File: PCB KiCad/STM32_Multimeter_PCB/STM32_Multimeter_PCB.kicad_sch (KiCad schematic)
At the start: 57 parts, among them J1 Conn_01x02_Pin, J2 USB_B_Micro, J3 Conn_01x04_Pin, J4 Conn_Coaxial, J5 Conn_01x03_Pin, SW1 SW_Push, SW3 SW_Push, SW4 SW_DPDT_x2, U1 STM32WB55CGUx, U10 AMS1117-3.3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

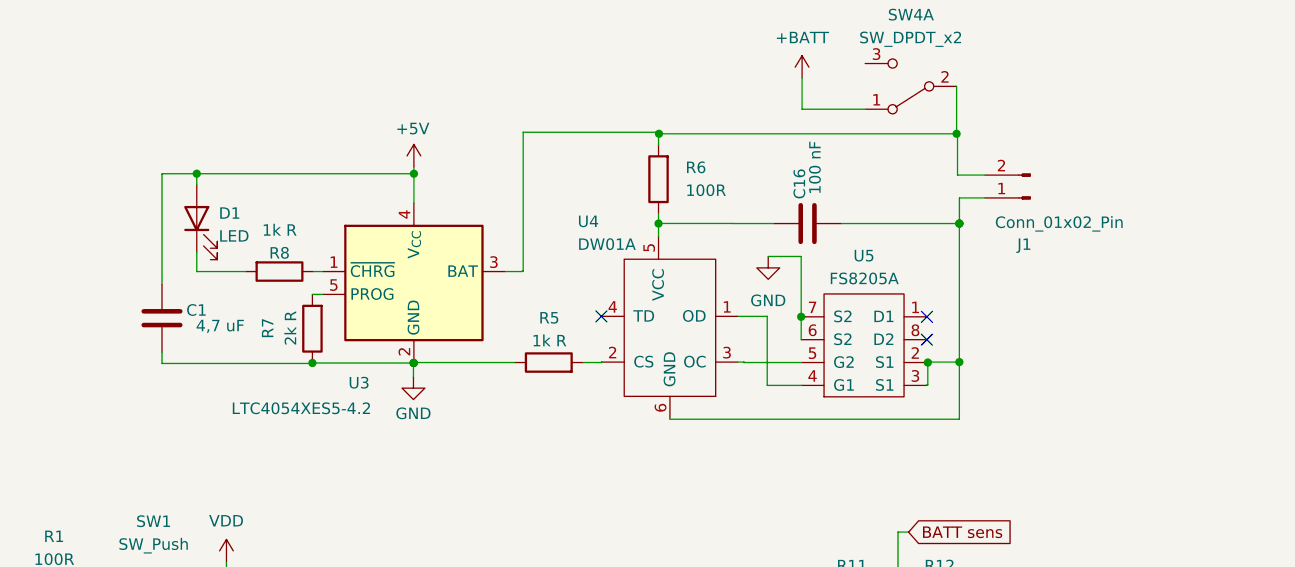
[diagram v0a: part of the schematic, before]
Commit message: Routed Analog and Microcontroler section
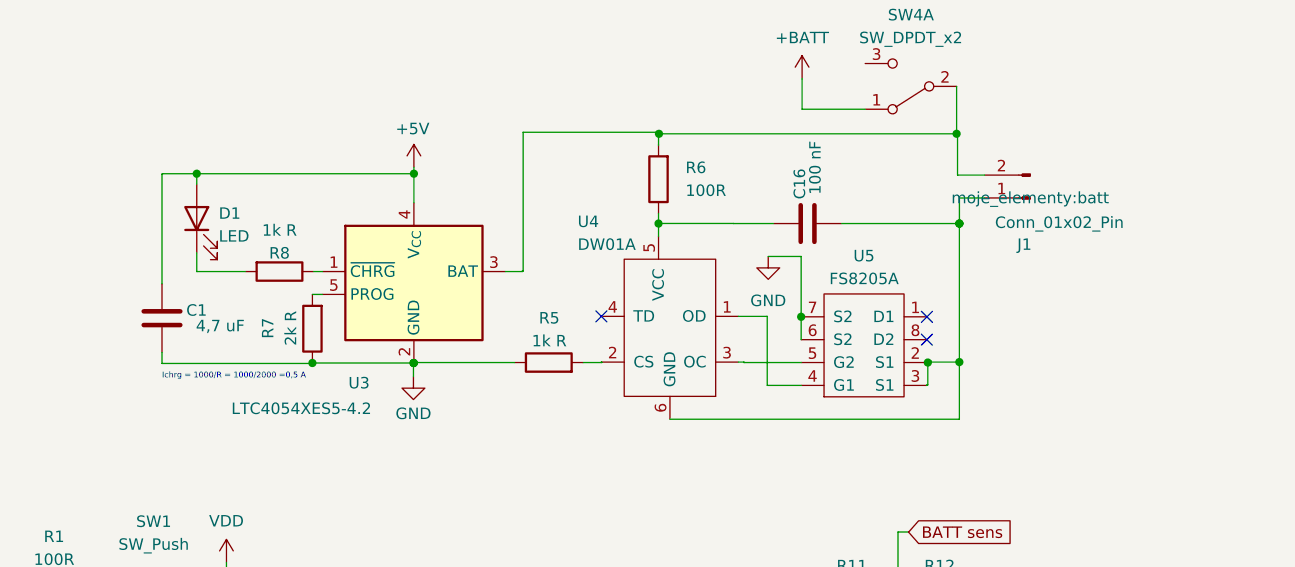
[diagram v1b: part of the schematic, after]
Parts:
- J1: footprint Connector_PinHeader_2.54mm:PinHeader_1x02_P2.54mm_Vertical -> moje_elementy:batt
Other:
- note added: "Ichrg = 1000/R = 1000/2000 =0,5 A"
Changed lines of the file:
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@@
     (stroke (width 0) (type default))
+  )
+  (text "Ichrg = 1000/R = 1000/2000 =0,5 A" (at 173.7868 54.2544 0)
+    (effects (font (size 0.64 0.64)) (justify left bottom))
   )
   (text "Lowpass filter \nfc=1/(2pi(LC)^1/2)=\n1/(2pi(10*10^-6*4,7*10^-6)^1/2)=\n23,22 kHz"
@@
       (effects (font (size 1.27 1.27)))
     )
-    (property "Footprint" "Connector_PinHeader_2.54mm:PinHeader_1x02_P2.54mm_Vertical" (at 270.256 33.9852 0)
-      (effects (font (size 1.27 1.27)) hide)
+    (property "Footprint" "moje_elementy:batt" (at 270.256 33.9852 0)
+      (effects (font (size 1.27 1.27)))
     )
     (property "Datasheet" "~" (at 270.256 33.9852 0)

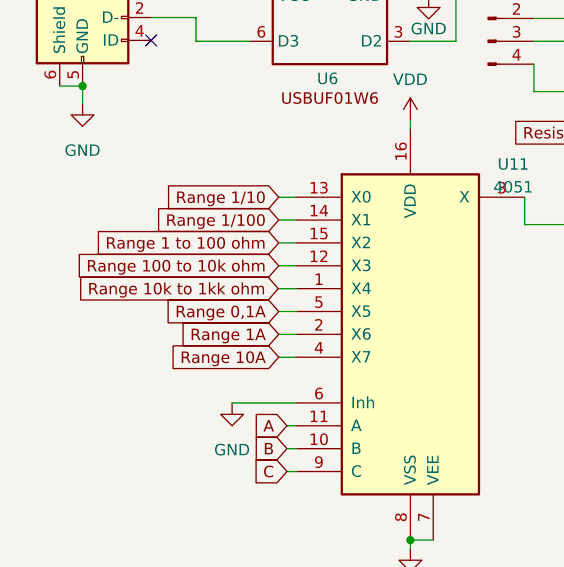
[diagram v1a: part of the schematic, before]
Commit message: routed out signals and power planes
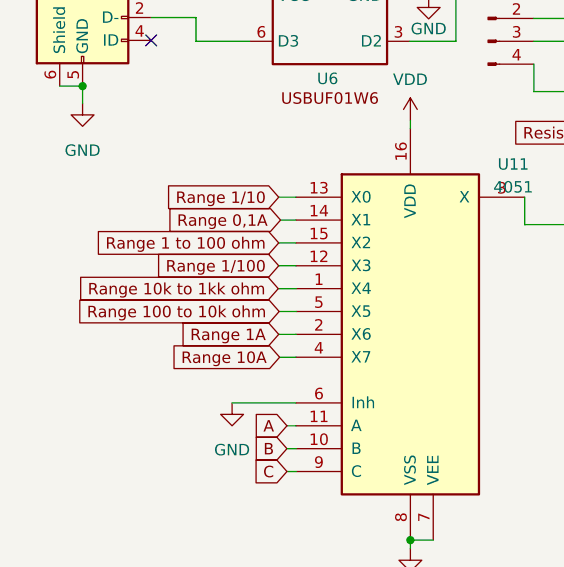
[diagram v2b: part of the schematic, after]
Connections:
- net Range 0,1A: now also U11.14 (X1); no longer U11.5 (X5)
- net Range 100 to 10k ohm: now also U11.5 (X5); no longer U11.12 (X3)
- net Range 1/100: now also U11.12 (X3); no longer U11.14 (X1)
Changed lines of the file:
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@@
-    (stroke (width 0) (type default))
-  )
-  (wire (pts (xy 44.2468 151.5364) (xy 42.3164 151.5364))
     (stroke (width 0) (type default))
   )
@@
     (stroke (width 0) (type default))
   )
-  (wire (pts (xy 44.2468 159.1564) (xy 42.3164 159.1564))
+  (wire (pts (xy 42.3672 164.2364) (xy 44.2468 164.2364))
     (stroke (width 0) (type default))
   )
@@
     (stroke (width 0) (type default))
   )
+  (wire (pts (xy 42.418 169.3164) (xy 44.2468 169.3164))
+    (stroke (width 0) (type default))
+  )
   (wire (pts (xy 69.4944 32.9692) (xy 69.4944 32.3342))
     (stroke (width 0) (type default))
@@
     (stroke (width 0) (type default))
   )
+  (wire (pts (xy 42.5196 154.0764) (xy 44.2468 154.0764))
+    (stroke (width 0) (type default))
+  )
   (wire (pts (xy 47.752 114.4016) (xy 47.752 115.7732))
     (stroke (width 0) (type default))
@@
     (stroke (width 0) (type default))
   )
-  (wire (pts (xy 44.2468 154.0764) (xy 42.3164 154.0764))
-    (stroke (width 0) (type default))
-  )
   (wire (pts (xy 251.9172 24.13) (xy 244.9068 24.13))
     (stroke (width 0) (type default))
@@
     (stroke (width 0) (type default))
   )
-  (wire (pts (xy 44.2468 164.2364) (xy 42.3164 164.2364))
-    (stroke (width 0) (type default))
-  )
   (wire (pts (xy 122.5804 43.1371) (xy 122.5296 43.1371))
     (stroke (width 0) (type default))
@@
     (stroke (width 0) (type default))
   )
+  (wire (pts (xy 42.3164 159.1564) (xy 44.2468 159.1564))
+    (stroke (width 0) (type default))
+  )
   (wire (pts (xy 139.7508 121.5644) (xy 129.032 121.5644))
     (stroke (width 0) (type default))
@@
     (stroke (width 0) (type default))
   )
-  (wire (pts (xy 42.3164 169.3164) (xy 44.2468 169.3164))
-    (stroke (width 0) (type default))
-  )
   (wire (pts (xy 29.8704 123.952) (xy 29.8704 122.2248))
     (stroke (width 0) (type default))
@@
   )
   (wire (pts (xy 87.7824 73.66) (xy 98.5012 73.66))
+    (stroke (width 0) (type default))
+  )
+  (wire (pts (xy 42.3164 151.5364) (xy 44.2468 151.5364))
     (stroke (width 0) (type default))
   )
@@
     (effects (font (size 0.54 0.54)) (justify left bottom))
   )
-  (global_label "Range 100 to 10k ohm" (shape input) (at 42.3164 159.1564 180) (fields_autoplaced)
-    (effects (font (size 1.27 1.27)) (justify right))
-    (property "Intersheetrefs" "${INTERSHEET_REFS}" (at 16.7136 159.1564 0)
+  (global_label "Range 100 to 10k ohm" (shape input) (at 42.3672 164.2364 180) (fields_autoplaced)
+    (effects (font (size 1.27 1.27)) (justify right))
+    (property "Intersheetrefs" "${INTERSHEET_REFS}" (at 16.7644 164.2364 0)
       (effects (font (size 1.27 1.27)) (justify right) hide)
     )
@@
     )
   )
-  (global_label "Range 1{slash}100" (shape input) (at 42.3164 154.0764 180) (fields_autoplaced)
-    (effects (font (size 1.27 1.27)) (justify right))
-    (property "Intersheetrefs" "${INTERSHEET_REFS}" (at 26.3895 154.0764 0)
-      (effects (font (size 1.27 1.27)) (justify right) hide)
-    )
-  )
-  (global_label "Range 0,1A" (shape input) (at 42.3164 164.2364 180) (fields_autoplaced)
-    (effects (font (size 1.27 1.27)) (justify right))
-    (property "Intersheetrefs" "${INTERSHEET_REFS}" (at 28.4456 164.2364 0)
+  (global_label "Range 1{slash}100" (shape input) (at 42.3164 159.1564 180) (fields_autoplaced)
+    (effects (font (size 1.27 1.27)) (justify right))
+    (property "Intersheetrefs" "${INTERSHEET_REFS}" (at 26.3895 159.1564 0)
+      (effects (font (size 1.27 1.27)) (justify right) hide)
+    )
+  )
+  (global_label "Range 0,1A" (shape input) (at 42.5196 154.0764 180) (fields_autoplaced)
+    (effects (font (size 1.27 1.27)) (justify right))
+    (property "Intersheetrefs" "${INTERSHEET_REFS}" (at 28.6488 154.0764 0)
       (effects (font (size 1.27 1.27)) (justify right) hide)
     )
@@
     )
   )
-  (global_label "Range 10A" (shape input) (at 42.3164 169.3164 180) (fields_autoplaced)
-    (effects (font (size 1.27 1.27)) (justify right))
-    (property "Intersheetrefs" "${INTERSHEET_REFS}" (at 29.0504 169.3164 0)
-      (effects (font (size 1.27 1.27)) (justify right) hide)
-    )
+  (global_label "Range 10A" (shape input) (at 42.418 169.3164 180) (fields_autoplaced)
+    (effects (font (size 1.27 1.27)) (justify right))
+    (property "Intersheetrefs" "${INTERSHEET_REFS}" (at 29.152 169.3164 0)
+      (effects (font (size 1.27 1.27)) (justify right) hide)
+    )

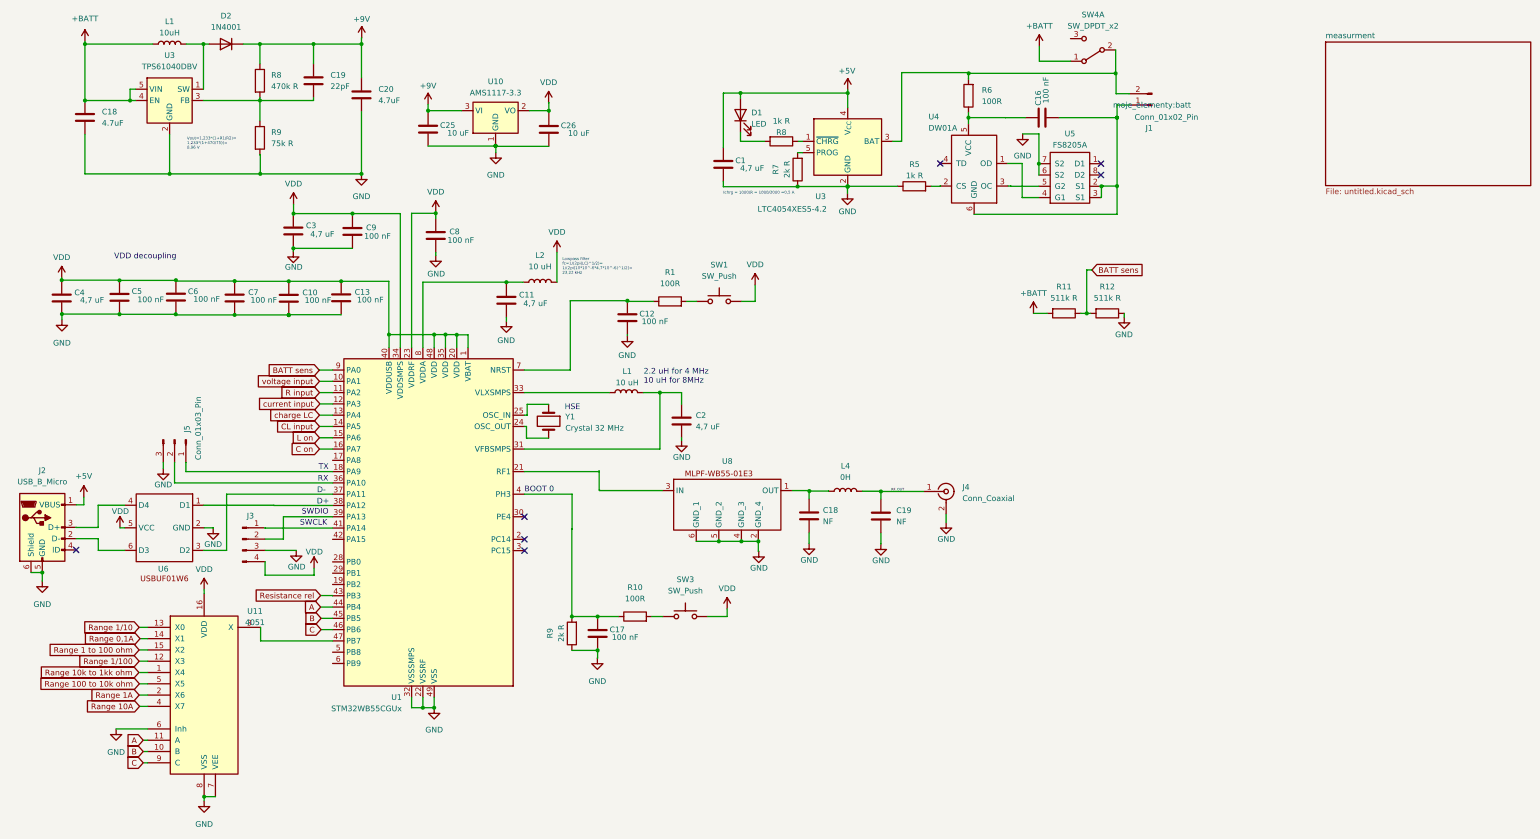
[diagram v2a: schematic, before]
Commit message: added i2c for oled and 2 buttons to pcb
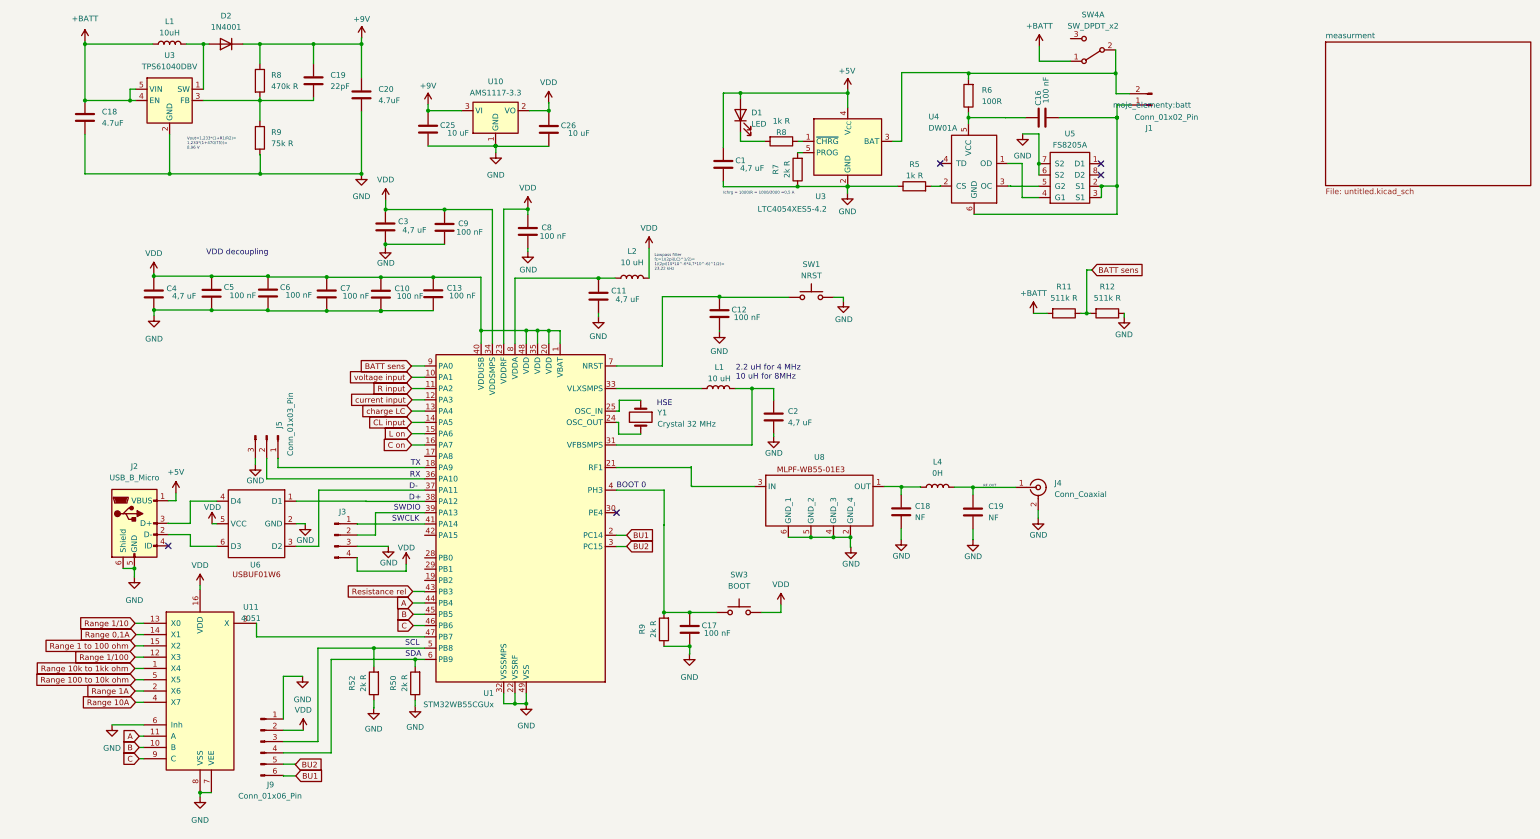
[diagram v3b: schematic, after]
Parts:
- removed R1, R10: 100R, Resistor_SMD:R_0805_2012Metric, symbol Device:R
- added J9: Conn_01x06_Pin, Connector_PinHeader_2.54mm:PinHeader_1x06_P2.54mm_Vertical, symbol Connector:Conn_01x06_Pin
- added R50, R52: 2k R, Resistor_SMD:R_0805_2012Metric, symbol Device:R
- SW1: value SW_Push -> NRST
- SW3: value SW_Push -> BOOT
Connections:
- net GND: now also SW1.2, J9.1 (Pin_1), R50.1, R52.1
- net VDD: now also J9.2 (Pin_2); no longer SW1.2
- net at C17.2, R9.2, U1.4 (PH3): now also SW3.1
- net at SW1.1: now also C12.2, U1.7 (NRST)
- net BU1: now reaches U1.2 (PC14)
- net BU1: now also J9.6 (Pin_6)
- net BU2: now reaches U1.3 (PC15)
- net BU2: now also J9.5 (Pin_5)
- net at U1.5 (PB8): now also J9.3 (Pin_3), R52.2
- net at U1.6 (PB9): now also J9.4 (Pin_4), R50.2
- no-connect marks 7 -> 5
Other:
- note added: "SCL"
- note added: "SDA"
- moved on the sheet: C10, C11, C12, C13, C17, C18, C19, C2, C3, C4, C5, C6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

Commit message: added missing shop links to the part list
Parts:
- removed Y1: Crystal 32 MHz, Crystal:Crystal_SMD_5032-2Pin_5.0x3.2mm_HandSoldering, symbol Device:Crystal
- added Y2: Crystal_GND24, Crystal:Crystal_SMD_3225-4Pin_3.2x2.5mm, symbol Device:Crystal_GND24
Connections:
- net GND: now also Y2.1, Y2.3
- net at U1.24 (OSC_OUT): now also Y2.4
- net at U1.25 (OSC_IN): now also Y2.2
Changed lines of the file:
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@@
     (stroke (width 0) (type default))
   )
-  (wire (pts (xy 149.7584 105.41) (xy 150.2156 105.41))
+  (wire (pts (xy 149.7584 105.41) (xy 151.7396 105.41))
     (stroke (width 0) (type default))
   )
@@
     (stroke (width 0) (type default))
   )
-  (wire (pts (xy 150.2156 108.0516) (xy 155.194 108.0516))
+  (wire (pts (xy 151.7396 109.4232) (xy 161.3916 109.4232))
     (stroke (width 0) (type default))
   )
@@
     (stroke (width 0) (type default))
   )
+  (wire (pts (xy 165.2016 104.3432) (xy 168.7576 104.3432))
+    (stroke (width 0) (type default))
+  )
   (wire (pts (xy 74.7776 184.9628) (xy 74.7776 184.8612))
     (stroke (width 0) (type default))
@@
     (stroke (width 0) (type default))
   )
-  (wire (pts (xy 150.368 100.4316) (xy 155.194 100.4316))
+  (wire (pts (xy 151.892 99.2632) (xy 161.3916 99.2632))
     (stroke (width 0) (type default))
   )
@@
     (stroke (width 0) (type default))
   )
+  (wire (pts (xy 157.5816 104.3432) (xy 155.4988 104.3432))
+    (stroke (width 0) (type default))
+  )
   (wire (pts (xy 213.8172 119.9388) (xy 213.8172 121.7168))
     (stroke (width 0) (type default))
@@
     (stroke (width 0) (type default))
   )
-  (wire (pts (xy 150.2156 105.41) (xy 150.2156 108.0516))
+  (wire (pts (xy 168.7576 104.3432) (xy 168.7576 104.4448))
+    (stroke (width 0) (type default))
+  )
+  (wire (pts (xy 151.7396 105.41) (xy 151.7396 109.4232))
     (stroke (width 0) (type default))
   )
@@
     (stroke (width 0) (type default))
   )
+  (wire (pts (xy 155.4988 104.3432) (xy 155.4988 104.2924))
+    (stroke (width 0) (type default))
+  )
   (wire (pts (xy 228.9548 36.83) (xy 228.9556 36.83))
     (stroke (width 0) (type default))
@@
     (stroke (width 0) (type default))
   )
-  (wire (pts (xy 149.7584 102.87) (xy 150.368 102.87))
+  (wire (pts (xy 149.7584 102.87) (xy 151.892 102.87))
     (stroke (width 0) (type default))
   )
@@
     (stroke (width 0) (type default))
   )
-  (wire (pts (xy 150.368 100.4316) (xy 150.368 102.87))
+  (wire (pts (xy 151.892 99.2632) (xy 151.892 102.87))
     (stroke (width 0) (type default))
   )
@@
     (effects (font (size 1.27 1.27) (color 0 0 0 1)) (justify left bottom))
   )
-  (text "HSE" (at 158.8008 101.9048 0)
+  (text "HSE" (at 162.56 100.5332 0)
     (effects (font (size 1.27 1.27) (color 0 0 0 1)) (justify left bottom))
   )
@@
     )
   )
+  (symbol (lib_id "Device:Crystal_GND24") (at 161.3916 104.3432 0) (unit 1)
+    (in_bom yes) (on_board yes) (dnp no) (fields_autoplaced)
+    (property "Reference" "Y2" (at 171.9072 100.1523 0)
+      (effects (font (size 1.27 1.27)))
+    )
+    (property "Value" "Crystal_GND24" (at 171.9072 102.6923 0)
+      (effects (font (size 1.27 1.27)))
+    )
+    (property "Footprint" "Crystal:Crystal_SMD_3225-4Pin_3.2x2.5mm" (at 161.3916 104.3432 0)
+      (effects (font (size 1.27 1.27)) hide)
+    )
+    (property "Datasheet" "~" (at 161.3916 104.3432 0)
+      (effects (font (size 1.27 1.27)) hide)
+    )
+    (pin "1")
+    (pin "2")
+    (pin "3")
+    (pin "4")
+    (instances
+      (project "STM32_Multimeter_PCB"
+        (path "/841997f8-2aac-4d7b-a188-492c61267162"
+          (reference "Y2") (unit 1)
+        )
+      )
+    )
+  )
   (symbol (lib_id "power:VDD") (at 45.6184 71.9328 0) (unit 1)
     (in_bom yes) (on_board yes) (dnp no) (fields_autoplaced)
@@
     )
   )
-  (symbol (lib_id "Device:Crystal") (at 155.194 104.2416 270) (unit 1)
-    (in_bom yes) (on_board yes) (dnp no)
-    (property "Reference" "Y1" (at 158.9532 103.2256 90)
-      (effects (font (size 1.27 1.27)) (justify left))
-    )
-    (property "Value" "Crystal 32 MHz" (at 158.9532 105.7656 90)
-      (effects (font (size 1.27 1.27)) (justify left))
-    )
-    (property "Footprint" "Crystal:Crystal_SMD_5032-2Pin_5.0x3.2mm_HandSoldering" (at 155.194 104.2416 0)
-      (effects (font (size 1.27 1.27)) hide)
-    )
-    (property "Datasheet" "~" (at 155.194 104.2416 0)
-      (effects (font (size 1.27 1.27)) hide)
-    )
-    (pin "1")
-    (pin "2")
-    (instances
-      (project "STM32_Multimeter_PCB"
-        (path "/841997f8-2aac-4d7b-a188-492c61267162"
-          (reference "Y1") (unit 1)
-        )
-      )
-    )
-  )
   (symbol (lib_id "power:GND") (at 202.4888 133.5024 0) (unit 1)
     (in_bom yes) (on_board yes) (dnp no)
@@
     )
   )
+  (symbol (lib_id "power:GND") (at 155.4988 104.2924 0) (unit 1)
+    (in_bom yes) (on_board yes) (dnp no)
+    (property "Reference" "#PWR071" (at 155.4988 110.6424 0)
+      (effects (font (size 1.27 1.27)) hide)
+    )
+    (property "Value" "GND" (at 155.448 108.6612 0)
+      (effects (font (size 1.27 1.27)))
+    )
+    (property "Footprint" "" (at 155.4988 104.2924 0)
+      (effects (font (size 1.27 1.27)) hide)
+    )
+    (property "Datasheet" "" (at 155.4988 104.2924 0)
+      (effects (font (size 1.27 1.27)) hide)
+    )
+    (pin "1")
+    (instances
+      (project "STM32_Multimeter_PCB"
+        (path "/841997f8-2aac-4d7b-a188-492c61267162"
+          (reference "#PWR071") (unit 1)
+        )
+      )
+    )
+  )
   (symbol (lib_id "power:GND") (at 95.0976 169.672 0) (unit 1)
     (in_bom yes) (on_board yes) (dnp no) (fields_autoplaced)
@@
         )
       )
+    )
+  )
+  (symbol (lib_id "power:GND") (at 168.7576 104.4448 0) (unit 1)
+    (in_bom yes) (on_board yes) (dnp no)
+    (property "Reference" "#PWR070" (at 168.7576 110.7948 0)
+      (effects (font (size 1.27 1.27)) hide)
+    )
+    (property "Value" "GND" (at 168.7068 108.8136 0)
+      (effects (font (size 1.27 1.27)))
+    )
+    (property "Footprint" "" (at 168.7576 104.4448 0)
+      (effects (font (size 1.27 1.27)) hide)
+    )
+    (property "Datasheet" "" (at 168.7576 104.4448 0)
+      (effects (font (size 1.27 1.27)) hide)
+    )
+    (pin "1")
+    (instances
+      (project "STM32_Multimeter_PCB"
+        (path "/841997f8-2aac-4d7b-a188-492c61267162"
+          (reference "#PWR070") (unit 1)
+        )
+      )
